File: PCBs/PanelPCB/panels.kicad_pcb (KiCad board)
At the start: 2 copper layers, 133 x 70.8 mm, 0 parts

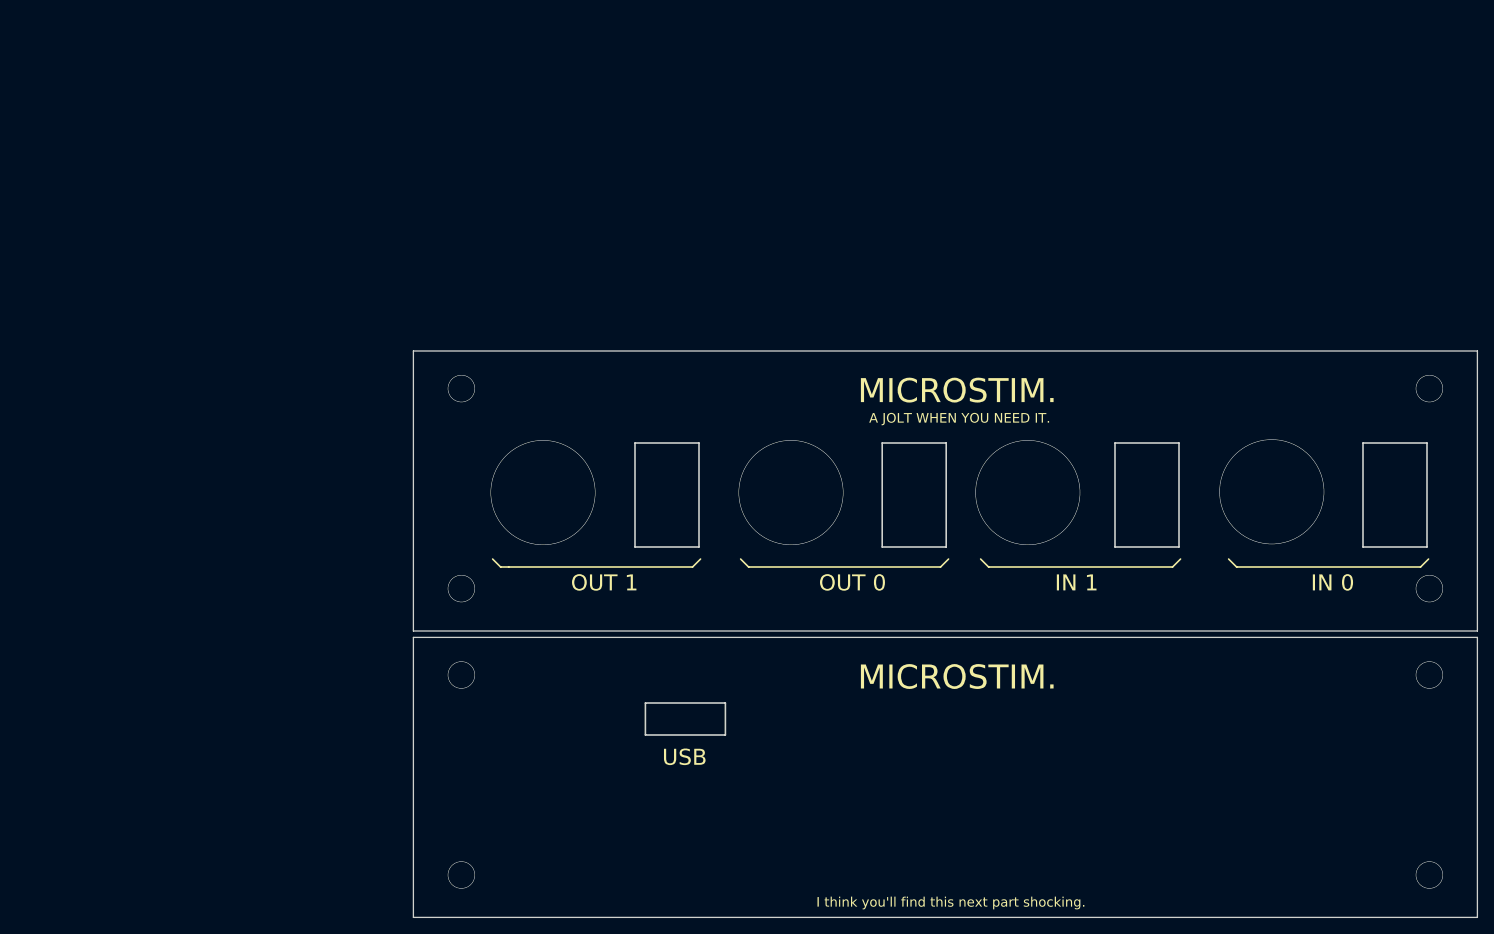
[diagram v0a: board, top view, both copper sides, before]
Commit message: boatload of updates via jons suggestions. de-isolated grounds via large resistors+capacitors (to prevent static buildup on animal or issues with large discharges). increased resistor values in voltage output non-inverting amplifier.
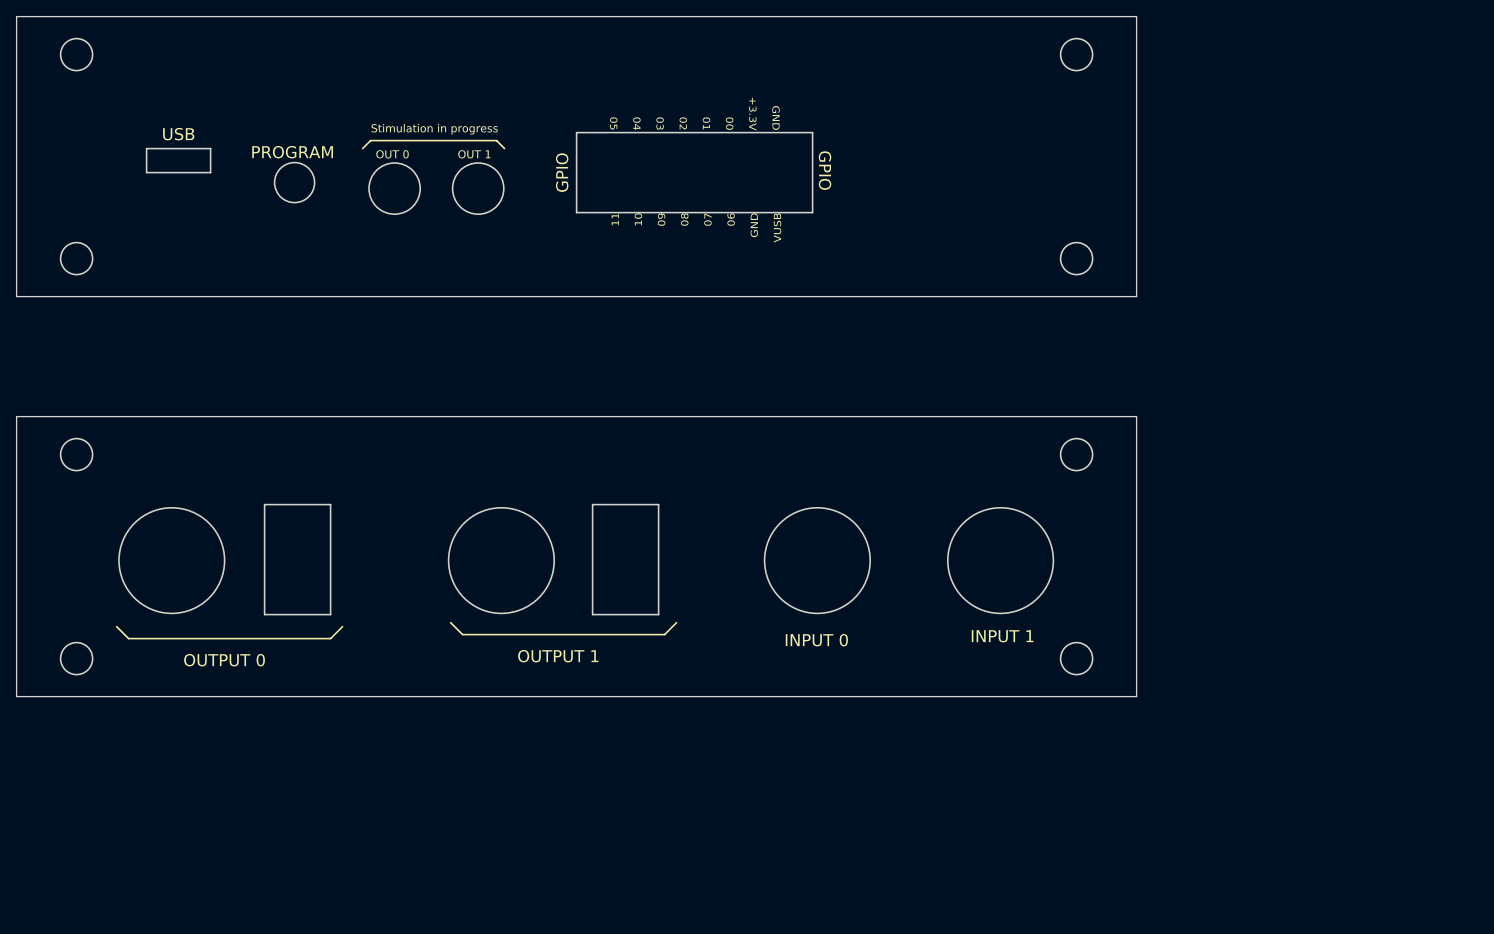
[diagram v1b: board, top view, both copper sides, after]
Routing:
- net (no net): vias 12 -> 0
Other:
- board size 133 x 70.8 mm -> 140 x 85 mm
- board text added: "11 10 09 08 07 06 GND VUSB"
- board text added: "GND +3.3V 00 01 02 03 04 05"
- board text added: "GPIO"
- board text added: "INPUT 0"
- board text added: "INPUT 1"
- board text added: "OUTPUT 0"
- board text added: "OUTPUT 1"
- board text added: "PROGRAM"
- board text added: "Stimulation in progress"
- board text removed: "A JOLT WHEN YOU NEED IT."
- board text removed: "I think you'll find this next part shocking."
- board text removed: "IN 0"
- board text removed: "IN 1"
- board text removed: "MICROSTIM."

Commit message: made combined pcb layout (panel+mainpcb), added fab files
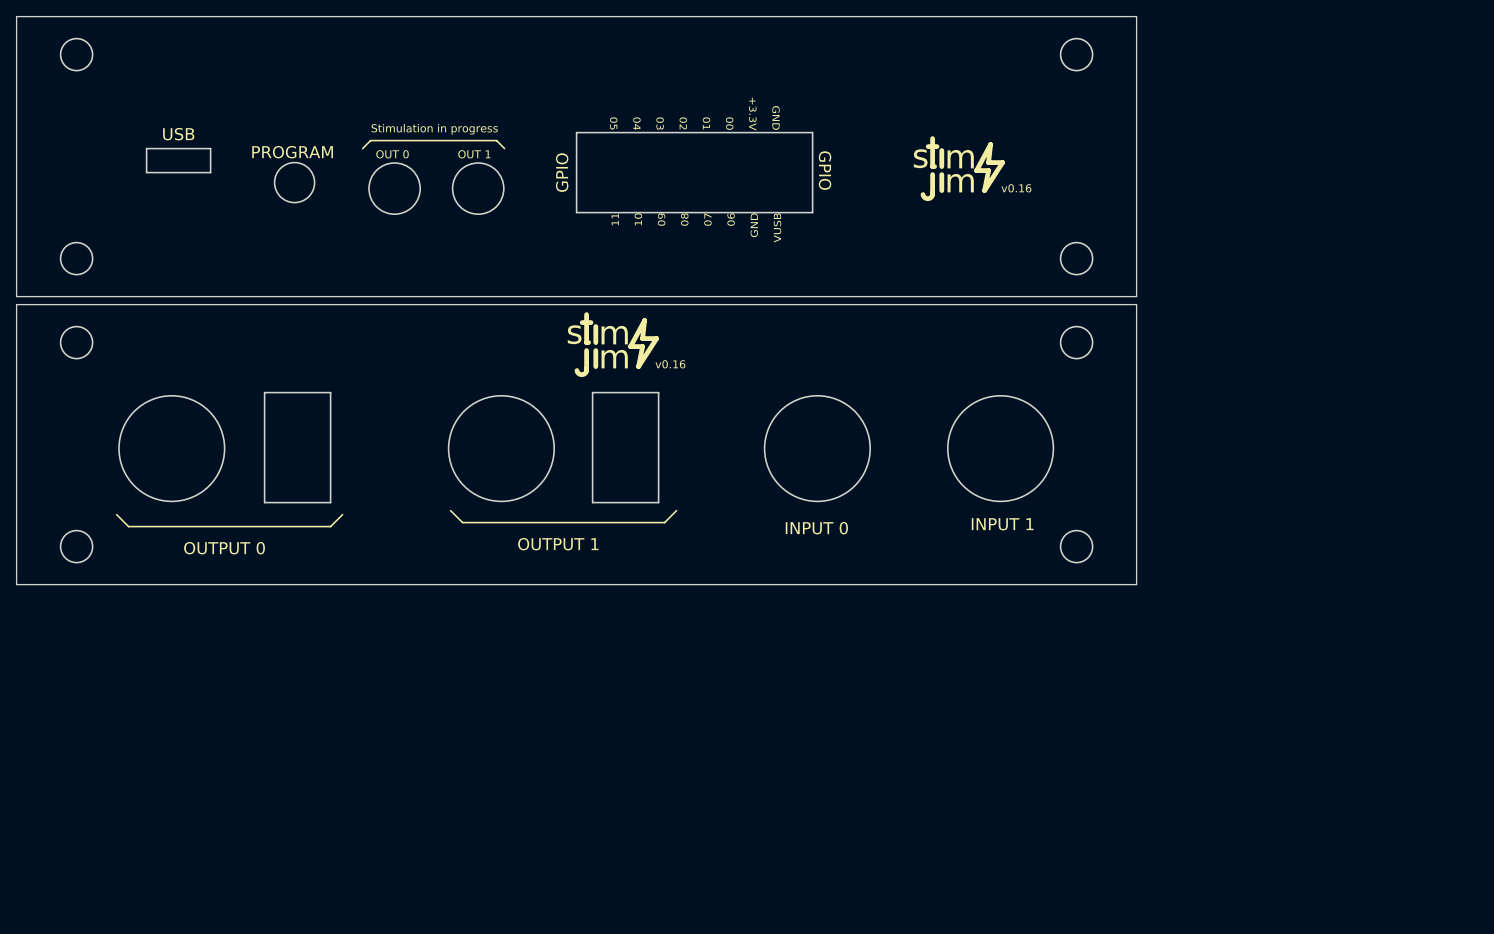
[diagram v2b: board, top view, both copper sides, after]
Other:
- board size 140 x 85 mm -> 140 x 71 mm
- net class Default: clearance 0.1524 -> 0.2
- net class thick added: clearance 0.2, trace_width 0.5, via_dia 1, via_drill 0.5
- rule pad_to_mask_clearance: 0.051 -> 0.2
- rule trace_clearance: 0.1524 -> 0.2
- board text added: "m"
- board text added: "s"
- board text added: "v0.16"
